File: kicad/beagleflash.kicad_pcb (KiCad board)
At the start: 2 copper layers, 86.4 x 54.6 mm, 27 parts, among them P1 SPI-8, P2 SPI-16, P3 BBB_P9, P4 BBB_P8, P5 EEPROM_PROG_EN, SW1 DIPS_02, U1 PAM2305, U2 74HC125, U3 CAT24C256W

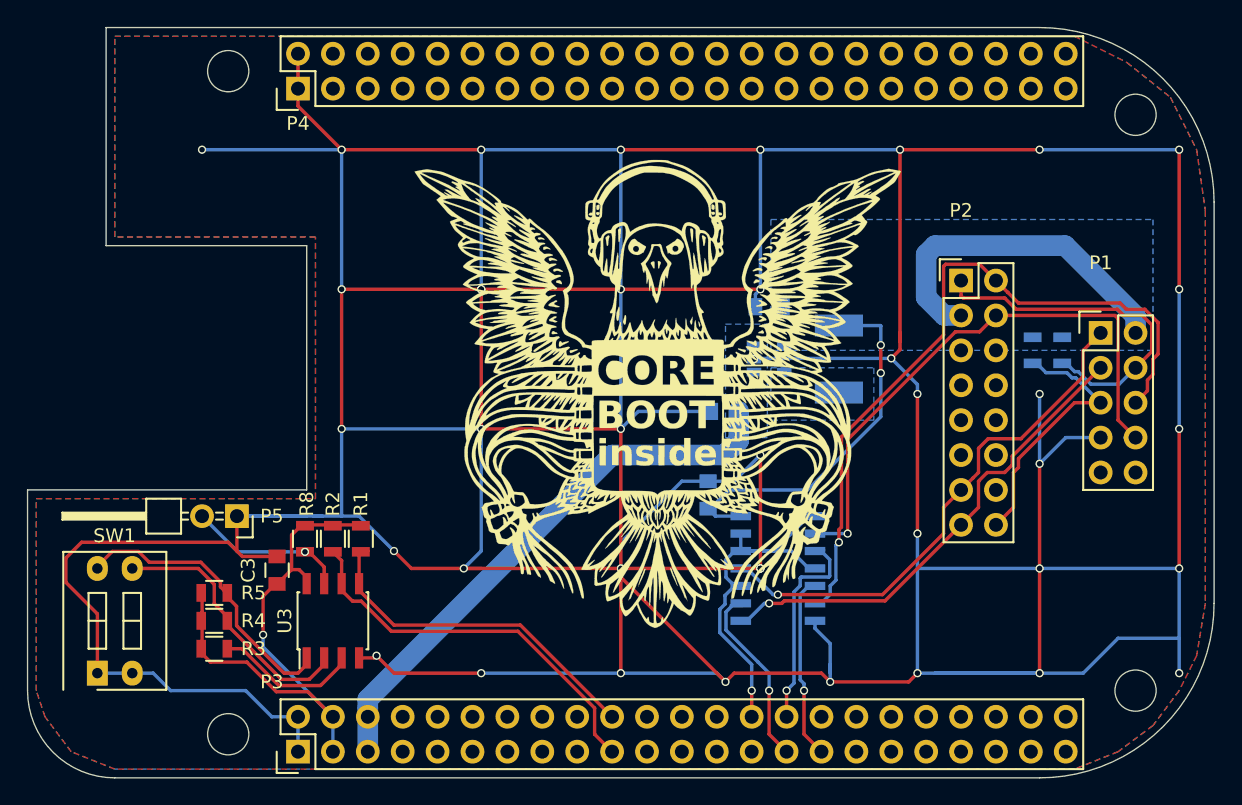
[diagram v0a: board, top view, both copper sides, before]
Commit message: kicad: Add Revision 0.2 of beagleflash
Previous revision did not work because the MOSI and MISO pins were
swapped before the buffer. That's now fixed. Other changes include:
 - Replaced individual resistors around EEPROM with resistor array
 - Added silkscreen designators for SPI pinout on 10-pin header
 - Re-organized DC-DC regulator to have shorter current loops
 - Added exposed GND copper around mounting holes.

Signed-off-by: Alexandru Gagniuc <mr.nuke.me@gmail.com>
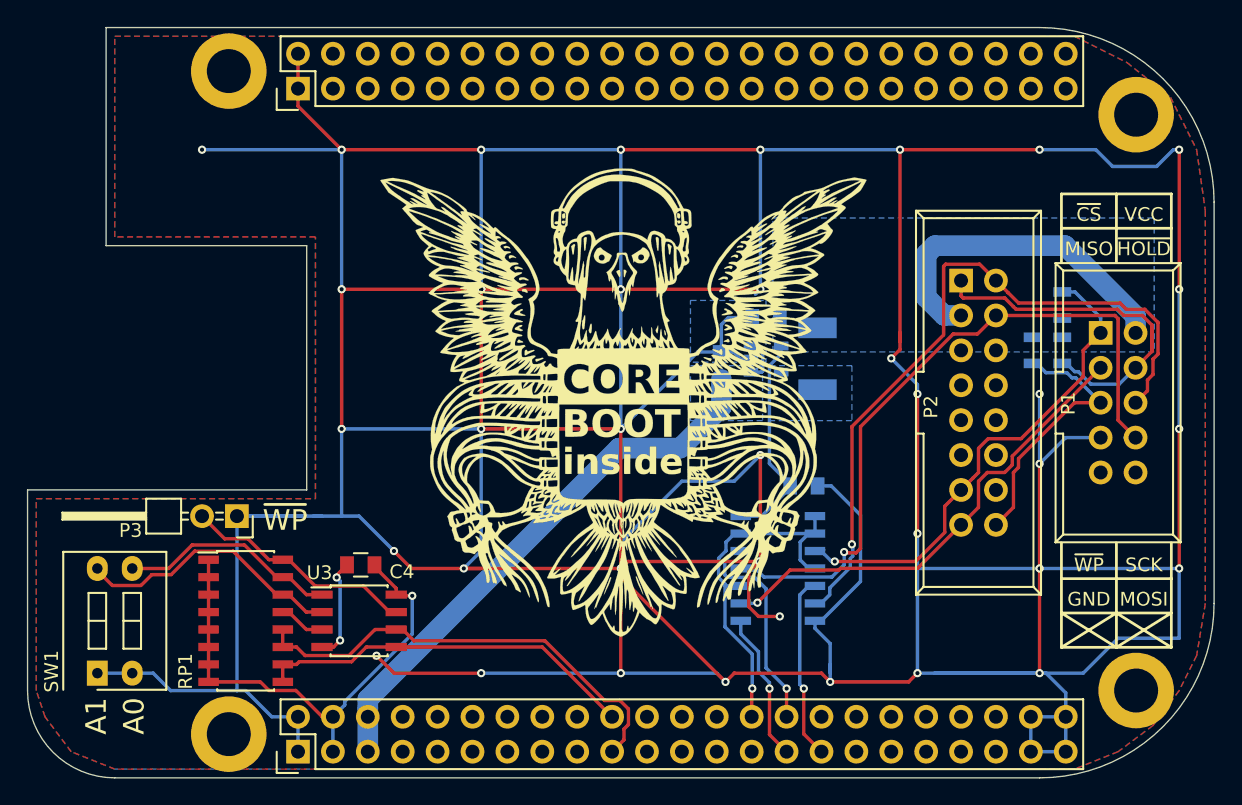
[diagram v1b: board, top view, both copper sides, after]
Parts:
- removed ? (x4): MountingHole_3mm, Mounting_Holes:MountingHole_3mm
- removed the G*** at (142.2, 83.8)
- removed R4, R5, R6, R7, R8: 10k, Resistors_SMD:R_0805
- added G***: LOGO, logo-coreboot, F.Cu at (139.7, 84.4)
- added P6: CONN_01X01, Mounting_Holes:MountingHole_3.2mm_M3_ISO14580_Pad, F.Cu at (111.2, 108.6)
- added P7: CONN_01X01, Mounting_Holes:MountingHole_3.2mm_M3_ISO14580_Pad, F.Cu at (111.2, 60.3)
- added P8: CONN_01X01, Mounting_Holes:MountingHole_3.2mm_M3_ISO14580_Pad, F.Cu at (177.2, 105.4)
- added P9: CONN_01X01, Mounting_Holes:MountingHole_3.2mm_M3_ISO14580_Pad, F.Cu at (177.2, 63.5)
- added RP1: 10k, Housings_SOIC:SOIC-16_3.9x9.9mm_Pitch1.27mm, F.Cu at (112.4, 100.3)
- C3: value 0.1uF -> 10uF; moved to B.Cu
- C4: value 10uF -> 0.1uF; moved to F.Cu
- L1: footprint Resistors_SMD:R_1812 -> Inductors_NEOSID:Neosid_Inductor_SM-NE45_SMD1812
- P1: footprint Pin_Headers:Pin_Header_Straight_2x05 -> Connect:IDC_Header_Straight_10pins
- P2: footprint Pin_Headers:Pin_Header_Straight_2x08 -> Connect:IDC_Header_Straight_16pins
- P3: value BBB_P9 -> EEPROM_PROG_EN; footprint Pin_Headers:Pin_Header_Straight_2x23 -> Pin_Headers:Pin_Header_Angled_2x01
- P4: value BBB_P8 -> BBB_P9
- P5: value EEPROM_PROG_EN -> BBB_P8; footprint Pin_Headers:Pin_Header_Angled_2x01 -> Pin_Headers:Pin_Header_Straight_2x23
- R1, R2: value 5.6k -> 10k; moved to B.Cu
- R3: moved to B.Cu
- U1: value PAM2305 -> PAM2305AAB330
- moved R3 65.4 mm to (171.8, 80.6), turned to 270 degrees
- moved R2 55.7 mm to (171.8, 77.3), turned to 90 degrees
- moved R1 50.8 mm to (169.7, 80.6)
- moved P4 48.3 mm to (116.2, 109.9)
- moved C3 38.8 mm to (153.0, 90.5), turned to 0 degrees
- moved P5 31.4 mm to (116.2, 61.6), turned to 90 degrees
- moved C4 25.8 mm to (120.8, 96.3), turned to 180 degrees
- moved P3 17.7 mm to (111.8, 92.7), turned to 180 degrees
- moved C1 3.34 mm to (147.0, 81.8), turned to 90 degrees
- moved U3 1.91 mm to (120.7, 100.3), turned to 0 degrees
- moved L1 1.56 mm to (154.0, 81.3)
- moved C2 0.82 mm to (150.3, 78.3)
- moved U1 0.22 mm to (150.3, 81.3)
- turned P1 to 270 degrees
- turned P2 to 270 degrees
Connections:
- C3 pad 1: +3V3 -> VCC
- C4 pad 1: VCC -> +3V3
- P1 pad 3: /CONN_DO -> /CONN_MISO
- P1 pad 8: /CONN_DI -> /CONN_MOSI
- P2 pad 15: /CONN_DO -> /CONN_MISO
- P2 pad 4: /CONN_DI -> /CONN_MOSI
- P3 pad 2: GND -> /~WP
- P4 pad 19: Net-(P4-Pad19) -> /I2C2_SCL
- P4 pad 20: Net-(P4-Pad20) -> /I2C2_SDA
- P4 pad 28: Net-(P4-Pad28) -> /~SPI_CS0
- P4 pad 29: Net-(P4-Pad29) -> /SPI_D0
- P4 pad 3: Net-(P4-Pad3) -> +3V3
- P4 pad 30: Net-(P4-Pad30) -> /SPI_D1
- P4 pad 31: Net-(P4-Pad31) -> /SPI_SCLK
- P4 pad 32: Net-(P4-Pad32) -> /VADC
- P4 pad 33: Net-(P4-Pad33) -> /AIN4
- P4 pad 34: Net-(P4-Pad34) -> /AGND
- P4 pad 35: Net-(P4-Pad35) -> /AIN6
- P4 pad 36: Net-(P4-Pad36) -> /AIN5
- P4 pad 37: Net-(P4-Pad37) -> /AIN2
- P4 pad 38: Net-(P4-Pad38) -> /AIN3
- P4 pad 39: Net-(P4-Pad39) -> /AIN0
- P4 pad 4: Net-(P4-Pad4) -> +3V3
- P4 pad 40: Net-(P4-Pad40) -> /AIN1
- P4 pad 43: Net-(P4-Pad43) -> GND
- P4 pad 44: Net-(P4-Pad44) -> GND
- P4 pad 45: Net-(P4-Pad45) -> GND
- P4 pad 46: Net-(P4-Pad46) -> GND
- P4 pad 5: Net-(P4-Pad5) -> +5V
- P4 pad 6: Net-(P4-Pad6) -> +5V
- P4 pad 7: Net-(P4-Pad7) -> /SYS_5V
- P4 pad 8: Net-(P4-Pad8) -> /SYS_5VB
- P5 pad 2: Net-(P5-Pad2) -> GND
- R1 pad 1: +3V3 -> VCC
- R1 pad 2: /I2C2_SDA -> /~CONN_WP
- R2 pad 1: +3V3 -> VCC
- R2 pad 2: /I2C2_SCL -> /~CONN_CS
- R3 pad 1: +3V3 -> VCC
- R3 pad 2: Net-(R3-Pad2) -> /~CONN_HOLD
- SW1 pad 3: Net-(R4-Pad2) -> /A0
- SW1 pad 4: Net-(R5-Pad2) -> /A1
- U2 pad 11: /~CONN_CS -> /CONN_MOSI
- U2 pad 12: /~SPI_CS0 -> /SPI_D1
- U2 pad 2: /CONN_DI -> /~SPI_CS0
- U2 pad 3: /SPI_D1 -> /~CONN_CS
- U2 pad 8: /CONN_DO -> /SPI_D0
- U2 pad 9: /SPI_D0 -> /CONN_MISO
- U3 pad 1: Net-(R5-Pad2) -> /A0
- U3 pad 2: Net-(R4-Pad2) -> /A1
- U3 pad 3: Net-(R3-Pad2) -> /A2
- U3 pad 7: Net-(P5-Pad2) -> /~WP
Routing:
- net /CONN_MOSI: track 0.00 -> 51.5 mm, vias 0 -> 1
- net /CONN_DI: track 42.7 -> 0.00 mm, vias 1 -> 0
- net /CONN_DO: track 35.3 -> 0.00 mm, vias 1 -> 0
- net /CONN_MISO: track 0.00 -> 35.2 mm, vias 0 -> 1
- net GND: track 580.0 -> 602.0 mm
- net Net-(R5-Pad2): track 21.9 -> 0.00 mm
- net /A1: track 0.00 -> 20.4 mm
- net Net-(R4-Pad2): track 19.4 -> 0.00 mm
- net /~WP: track 0.00 -> 17.0 mm
- net /A0: track 0.00 -> 16.0 mm
- net Net-(P5-Pad2): track 11.9 -> 0.00 mm, vias 1 -> 0
- net VCC: track 52.7 -> 40.8 mm, vias 2 -> 0
- net Net-(R3-Pad2): track 10.5 -> 0.00 mm
- net +3V3: track 43.6 -> 36.8 mm
- net /I2C2_SCL: track 28.7 -> 33.5 mm
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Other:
- net class Default: via_drill 0.4 -> 0.3
- net class POWER: via_drill 0.4 -> 0.3
- board text added: "A0"
- board text added: "A1"
- board text added: "GND"
- board text added: "MISO"
- board text added: "MOSI"
- board text added: "SCK"
- board text added: "VCC"
- board text added: "~CS"
- board text added: "~HOLD"
- board text added: "~WP"

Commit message: kicad: Add revision 0.3 layout
Signed-off-by: Alexandru Gagniuc <mr.nuke.me@gmail.com>
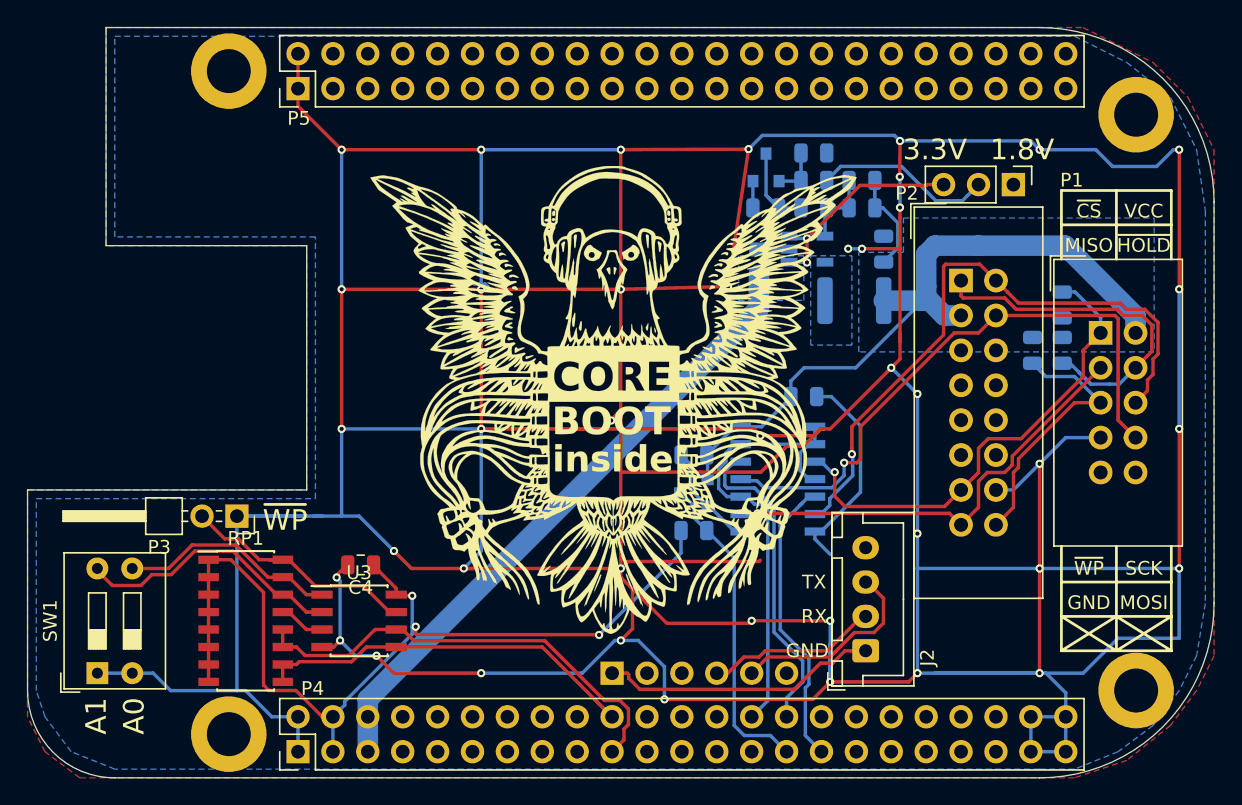
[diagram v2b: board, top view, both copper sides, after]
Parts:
- removed G***: LOGO, logo-coreboot
- removed P6, P7, P8, P9: CONN_01X01, Mounting_Holes:MountingHole_3.2mm_M3_ISO14580_Pad
- added C5: 100p, Capacitor_SMD:C_0805_2012Metric, B.Cu at (157.3, 68.3)
- added G1: Logo_Open_Hardware_Small, logo-coreboot, F.Cu at (139.0, 84.3)
- added H1: M3, MountingHole:MountingHole_3.2mm_M3_ISO14580_Pad, F.Cu at (111.2, 60.3)
- added H2: M3, MountingHole:MountingHole_3.2mm_M3_ISO14580_Pad, F.Cu at (111.2, 108.6)
- added H3: M3, MountingHole:MountingHole_3.2mm_M3_ISO14580_Pad, F.Cu at (177.2, 63.5)
- added H4: M3, MountingHole:MountingHole_3.2mm_M3_ISO14580_Pad, F.Cu at (177.2, 105.4)
- added J1: 6-pin socket, Connector_PinSocket_2.54mm:PinSocket_1x06_P2.54mm_Vertical, B.Cu at (139.1, 104.1)
- added J2: JST2.5, Connector_JST:JST_XH_B04B-XH-A_1x04_P2.50mm_Vertical, F.Cu at (157.5, 102.5)
- added Q1: BSS123, Package_TO_SOT_SMD:SOT-23, B.Cu at (145.0, 91.0)
- added Q2: BSS123, Package_TO_SOT_SMD:SOT-23, B.Cu at (150.3, 67.3)
- added R10: 10k, Resistor_SMD:R_0805_2012Metric, B.Cu at (153.8, 68.3)
- added R4: 10k, Resistor_SMD:R_0805_2012Metric, B.Cu at (145.0, 88.3)
- added R5: 10k, Resistor_SMD:R_0805_2012Metric, B.Cu at (145.0, 93.8)
- added R6: 47k, Resistor_SMD:R_0805_2012Metric, B.Cu at (157.3, 70.3)
- added R7: 10k, Resistor_SMD:R_0805_2012Metric, B.Cu at (153.8, 70.3)
- added R8: 15k, Resistor_SMD:R_0805_2012Metric, B.Cu at (150.3, 70.3)
- added R9: 47k, Resistor_SMD:R_0805_2012Metric, B.Cu at (153.8, 66.3)
- added SW2: SW_SPDT, Connector_PinHeader_2.54mm:PinHeader_1x03_P2.54mm_Vertical, F.Cu at (168.3, 68.6)
- C1, C2, C3, C4: footprint Capacitors_SMD:C_0805 -> Capacitor_SMD:C_0805_2012Metric
- L1: footprint Inductors_NEOSID:Neosid_Inductor_SM-NE45_SMD1812 -> Inductor_SMD:L_1812_4532Metric
- P1: footprint Connect:IDC_Header_Straight_10pins -> Connector_IDC:IDC-Header_2x05_P2.54mm_Vertical
- P2: footprint Connect:IDC_Header_Straight_16pins -> Connector_IDC:IDC-Header_2x08_P2.54mm_Vertical
- P3: footprint Pin_Headers:Pin_Header_Angled_2x01 -> Connector_PinHeader_2.54mm:PinHeader_2x01_P2.54mm_Horizontal
- P4, P5: footprint Pin_Headers:Pin_Header_Straight_2x23 -> Connector_PinHeader_2.54mm:PinHeader_2x23_P2.54mm_Vertical
- R1, R2, R3: footprint Resistors_SMD:R_0805 -> Resistor_SMD:R_0805_2012Metric
- RP1: footprint Housings_SOIC:SOIC-16_3.9x9.9mm_Pitch1.27mm -> Package_SO:SOIC-16_3.9x9.9mm_P1.27mm
- SW1: footprint Buttons_Switches_ThroughHole:SW_DIP_x2_Slide -> Button_Switch_THT:SW_DIP_SPSTx02_Slide_9.78x7.26mm_W7.62mm_P2.54mm
- U1: footprint TO_SOT_Packages_SMD:SOT-23-5 -> Package_TO_SOT_SMD:TSOT-23-5
- U2: footprint Housings_SOIC:SOIC-14_3.9x8.7mm_Pitch1.27mm -> Package_SO:SOIC-14_3.9x8.7mm_P1.27mm
- U3: footprint Housings_SOIC:SOIC-8_3.9x4.9mm_Pitch1.27mm -> Package_SO:SOIC-8_3.9x4.9mm_P1.27mm
- moved C2 9.91 mm to (158.8, 73.3), turned to 90 degrees
- moved U1 8.54 mm to (153.3, 73.3)
- moved C1 8.02 mm to (149.8, 74.2)
- moved C3 6.50 mm to (153.0, 84.0)
- moved U2 6.50 mm to (151.1, 90.0)
- moved L1 5.01 mm to (156.7, 77.0), turned to 0 degrees
- turned P1 to 0 degrees
- turned P2 to 0 degrees
- turned SW1 to 90 degrees
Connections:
- U1 pad 4: VCC -> Net-(C5-Pad2)
- U2 pad 8: /SPI_D0 -> Net-(Q1-Pad2)
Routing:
- net +3V3: track 36.8 -> 68.6 mm, vias 1 -> 3
- net Net-(J1-Pad1): track 0.00 -> 20.3 mm
- net +5V: track 43.7 -> 62.5 mm, vias 0 -> 2
- net VCC: track 40.8 -> 58.8 mm
- net /UART_TX: track 0.00 -> 14.7 mm
- net /SPI_D0: track 10.9 -> 23.9 mm, vias 1 -> 0
- net Net-(R10-Pad2): track 0.00 -> 13.0 mm
- net /UART_RX: track 0.00 -> 12.5 mm
- net GND: track 602.0 -> 610.9 mm, vias 40 -> 41
- net /SPI_SCLK: track 13.8 -> 22.0 mm, vias 1 -> 0
- net Net-(Q1-Pad2): track 0.00 -> 7.72 mm
- net /SPI_D1: track 15.8 -> 23.4 mm, vias 1 -> 0
- net /~SPI_CS0: track 28.4 -> 35.8 mm, vias 1 -> 0
- net Net-(Q2-Pad3): track 0.00 -> 7.10 mm
- net /CONN_MOSI: track 51.5 -> 44.9 mm
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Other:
- board text added: "1.8V"
- board text added: "3.3V"
- board text added: "RX"
- board text added: "TX"
